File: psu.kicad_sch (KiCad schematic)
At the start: 29 parts, among them U15 TPS563201DDCR, U16 LM1117-ADJ, U17 LM1117-ADJ

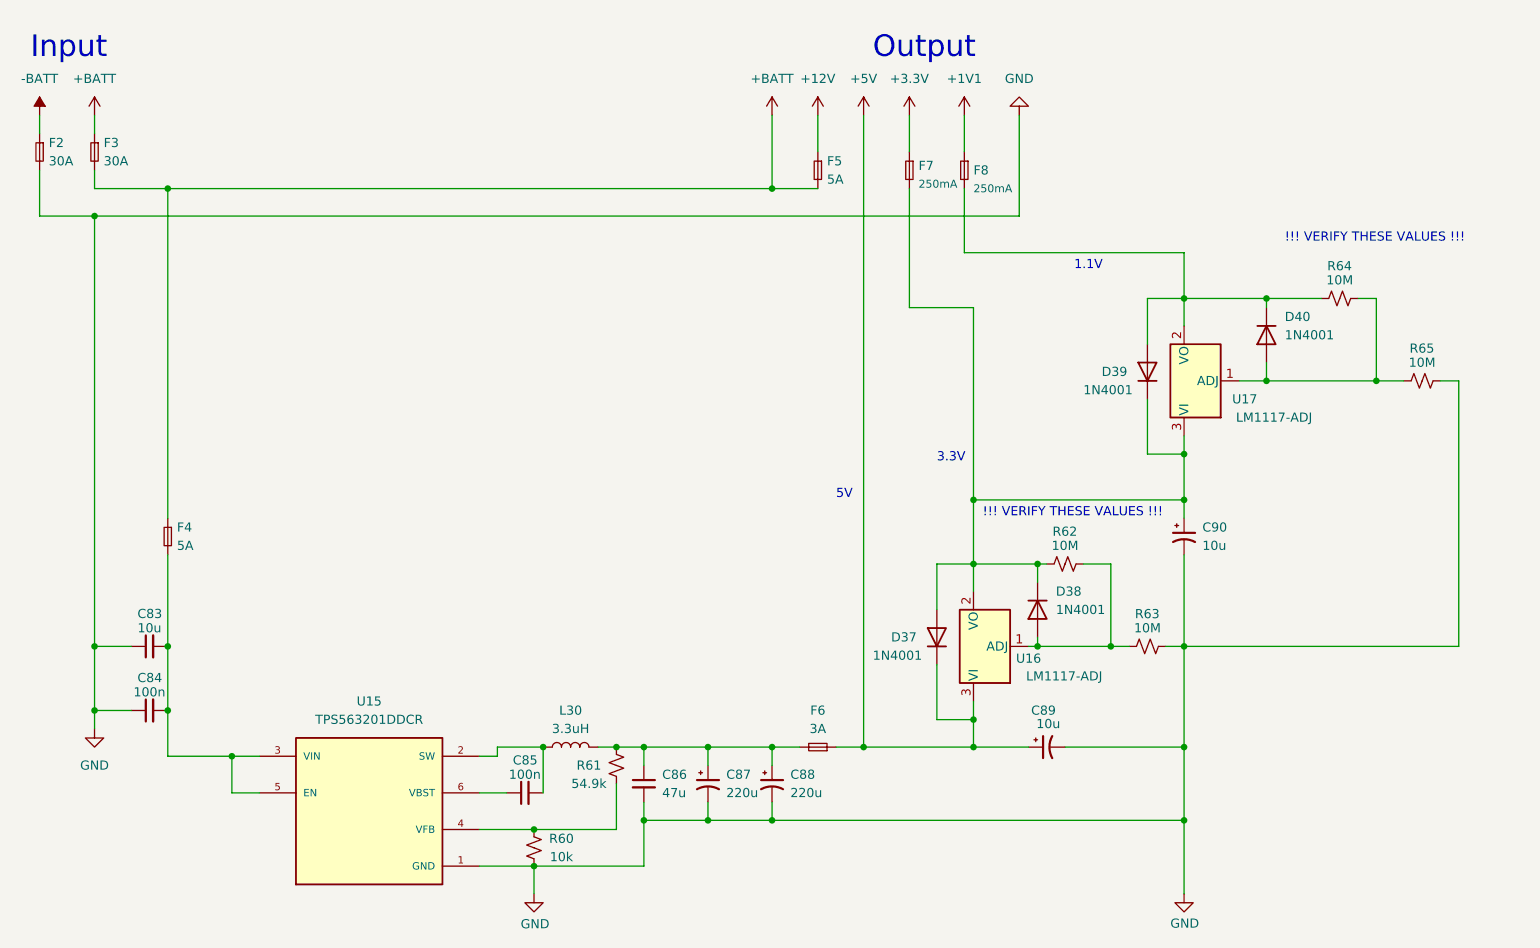
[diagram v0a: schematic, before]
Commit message: Replaced 74hc596 parts with mcp23017 and mcp23008 parts to simplify routing and reduce external parts count.
Added interface connectors for eventualy VHF (6m/2m/1.25m) RF path board.

Attempted to create some sort of documentations...
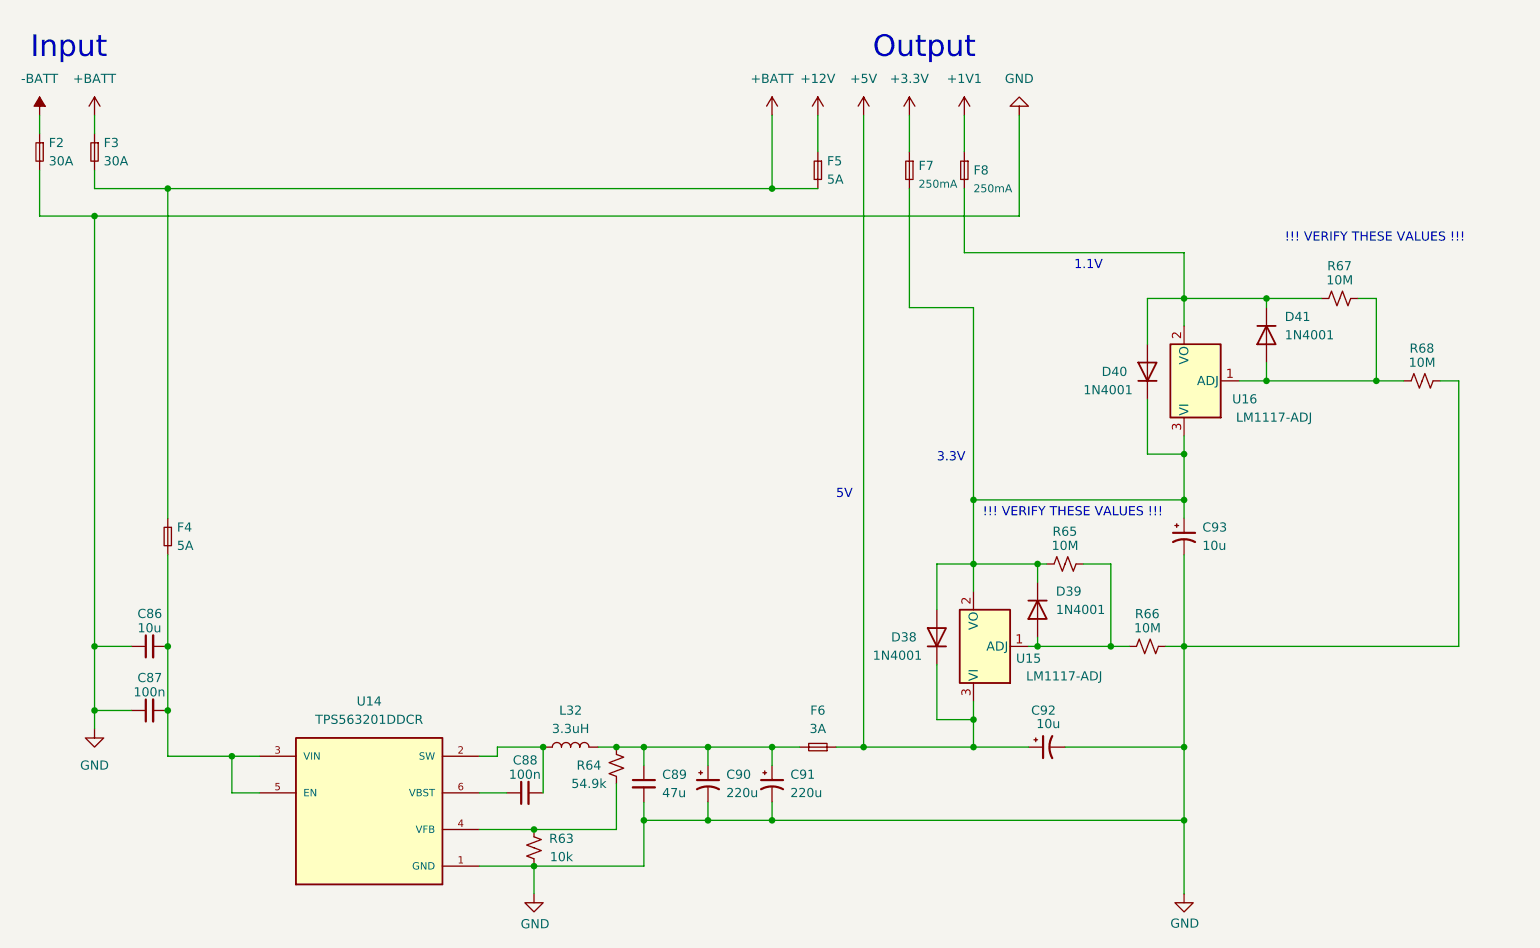
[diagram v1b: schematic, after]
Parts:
- renumbered C83 to C86, C84 to C87, C85 to C88, C86 to C89, C87 to C90, C88 to C91, C89 to C92, C90 to C93, D37 to D38, D38 to D39, D39 to D40, D40 to D41, L30 to L32, R60 to R63, R61 to R64, R62 to R65, R63 to R66, R64 to R67, R65 to R68, U15 to U14, U16 to U15, U17 to U16

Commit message: cleanup of schematic and some initial firmware works...
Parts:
- removed C86: 10u, Capacitor_THT:C_Disc_D4.7mm_W2.5mm_P5.00mm, symbol Device:C_Small
- removed C87, C88: 100n, Capacitor_THT:C_Disc_D4.7mm_W2.5mm_P5.00mm, symbol Device:C_Small
- removed C89: 47u, Capacitor_THT:C_Disc_D4.7mm_W2.5mm_P5.00mm, symbol Device:C_Small
- removed C90, C91: 220u, Capacitor_THT:CP_Radial_D4.0mm_P2.00mm, symbol Device:C_Polarized_Small_US
- removed C92, C93: 10u, Capacitor_THT:CP_Radial_D4.0mm_P2.00mm, symbol Device:C_Polarized_Small_US
- removed D38, D39, D40, D41: 1N4001, Diode_THT:D_DO-41_SOD81_P10.16mm_Horizontal, symbol Diode:1N4001
- removed F4: 5A, Fuse:Fuseholder_Blade_Mini_Keystone_3568, symbol Device:Fuse_Small
- removed L32: 3.3uH, symbol Device:L
- removed R63: 10k, Resistor_THT:R_Axial_DIN0207_L6.3mm_D2.5mm_P2.54mm_Vertical, symbol Device:R_Small_US
- removed R64: 54.9k, Resistor_THT:R_Axial_DIN0207_L6.3mm_D2.5mm_P2.54mm_Vertical, symbol Device:R_Small_US
- removed R65, R66, R67: 10M, Resistor_THT:R_Axial_DIN0207_L6.3mm_D2.5mm_P2.54mm_Vertical, symbol Device:R_Small_US
- removed U14: TPS563201DDCR, SOT95P280X110-6N, symbol TPS563201DDCR:TPS563201DDCR
- removed U15, U16: LM1117-ADJ, symbol Regulator_Linear:LM1117-ADJ
- added C96, C97: 10u, Capacitor_THT:CP_Radial_D4.0mm_P2.00mm, symbol Device:C_Polarized_Small_US
- added D43, D44, D45, D46: 1N4001, Diode_THT:D_DO-41_SOD81_P10.16mm_Horizontal, symbol Diode:1N4001
- added R69, R70, R71: 10M, Resistor_THT:R_Axial_DIN0207_L6.3mm_D2.5mm_P2.54mm_Vertical, symbol Device:R_Small_US
- added U13, U14: LM1117-ADJ, symbol Regulator_Linear:LM1117-ADJ
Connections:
- net +5V: now also F6.2; no longer F6.1
- net GND: now also C96.2, C97.2, R69.2, R71.2; no longer R68.2
- net at F8.2: now also D45.2 (A), D46.1 (K), R70.1, U14.2 (VO)
- net at F7.2: now also R68.1, C97.1, D43.2 (A), D44.1 (K), D45.1 (K), U13.2 (VO), U14.3 (VI)
- new net: C96.1, D43.1 (K), F6.1, U13.3 (VI)
- new net: D46.2 (A), R70.2, R71.1, U14.1 (ADJ)
- new net: D44.2 (A), R68.2, R69.1, U13.1 (ADJ)
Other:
- note removed: "5V"
